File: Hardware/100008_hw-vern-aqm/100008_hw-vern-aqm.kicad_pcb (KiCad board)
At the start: 2 copper layers, 98 x 56.3 mm, 82 parts, among them J1 Conn_01x14_Socket, J2 USB4220-03-1000-C, J3 Conn_01x06_MountingPin, J4 Conn_01x03_Pin, J5 Conn_01x06_Socket, J6 Conn_01x04_Socket, J7 Conn_01x05_Pin, J8 Conn_01x04_MountingPin, Q1 BC817, Q2 BC817, SW1 SW_Push, SW2 SW_Push, U1 AMS1117-3.3, U2 ESP32-S3-WROOM-1, U3 CP2102N-Axx-xQFN24, U4 SCD40-D-R2, U5 DPS368

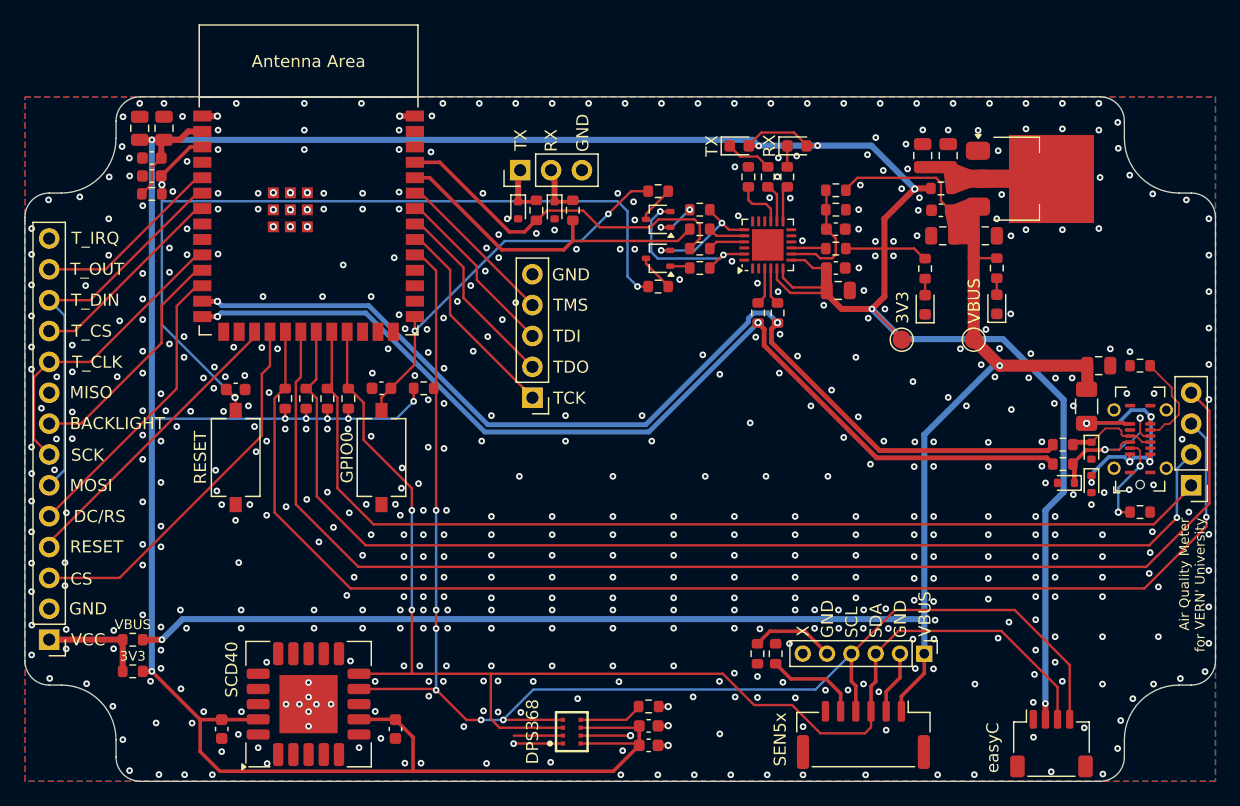
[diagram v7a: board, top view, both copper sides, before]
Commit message: fixing DRC issues
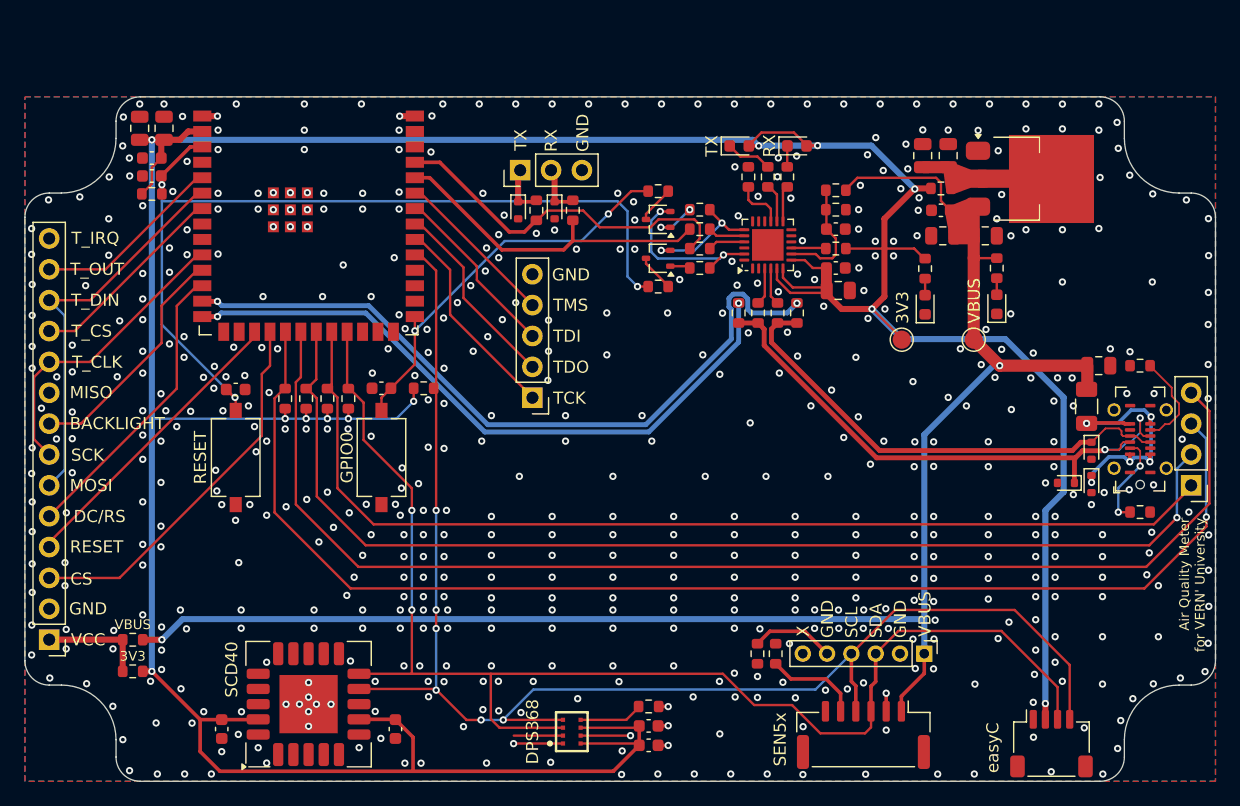
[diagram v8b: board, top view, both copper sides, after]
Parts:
- moved R5 28.8 mm to (158.8, 317.8), turned to 90 degrees
- moved R6 25.2 mm to (163.6, 317.8), turned to 90 degrees
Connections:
- D2 pad 1: Net-(D2-K) -> USB_D-
- D3 pad 1: Net-(D3-K) -> USB_D+
- J2 pad A6: Net-(D3-K) -> USB_D+
- J2 pad A7: Net-(D2-K) -> USB_D-
- J2 pad B6: Net-(D3-K) -> USB_D+
- J2 pad B7: Net-(D2-K) -> USB_D-
- R5 pad 1: Net-(D2-K) -> USB_D+
- R5 pad 2: USB_D- -> Net-(U2-GPIO20/U1CTS/ADC2_CH9/CLK_OUT1/USB_D+)
- R6 pad 1: Net-(D3-K) -> USB_D-
- R6 pad 2: USB_D+ -> Net-(U2-GPIO19/U1RTS/ADC2_CH8/CLK_OUT2/USB_D-)
- U2 pad 13: USB_D- -> Net-(U2-GPIO19/U1RTS/ADC2_CH8/CLK_OUT2/USB_D-)
- U2 pad 14: USB_D+ -> Net-(U2-GPIO20/U1CTS/ADC2_CH9/CLK_OUT1/USB_D+)
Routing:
- net Net-(U2-GPIO19/U1RTS/ADC2_CH8/CLK_OUT2/USB_D-): track 0.00 -> 62.0 mm, vias 0 -> 2
- net Net-(U2-GPIO20/U1CTS/ADC2_CH9/CLK_OUT1/USB_D+): track 0.00 -> 55.2 mm, vias 0 -> 2
- net USB_D-: track 85.4 -> 39.7 mm, vias 2 -> 0
- net USB_D+: track 84.1 -> 47.1 mm
- net Net-(D3-K): track 13.9 -> 0.00 mm, vias 2 -> 0
- net Net-(D2-K): track 7.54 -> 0.00 mm
- net GND: track 18.4 -> 14.7 mm, vias 562 -> 574
